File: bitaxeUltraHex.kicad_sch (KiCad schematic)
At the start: 10 parts, among them J1 Screw Terminal, J2 Conn_01x01

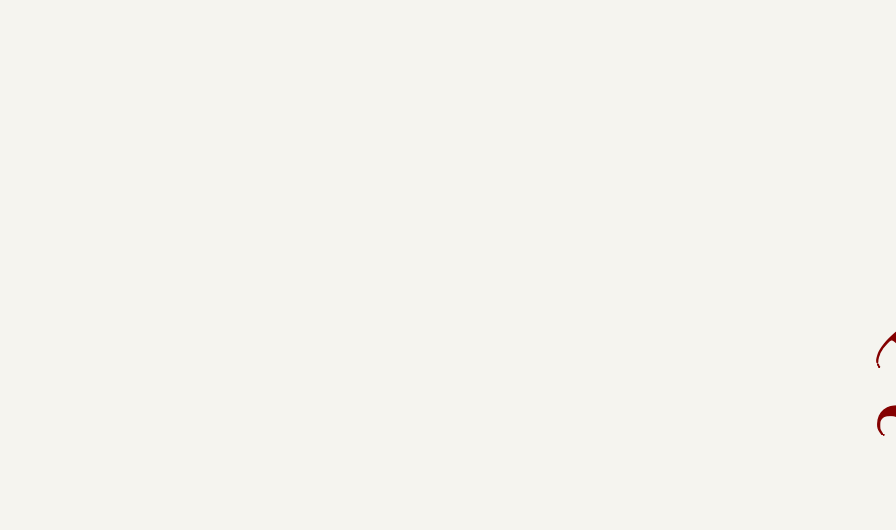
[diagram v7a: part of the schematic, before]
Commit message: re added mounting holes and heatsink mounting holes.
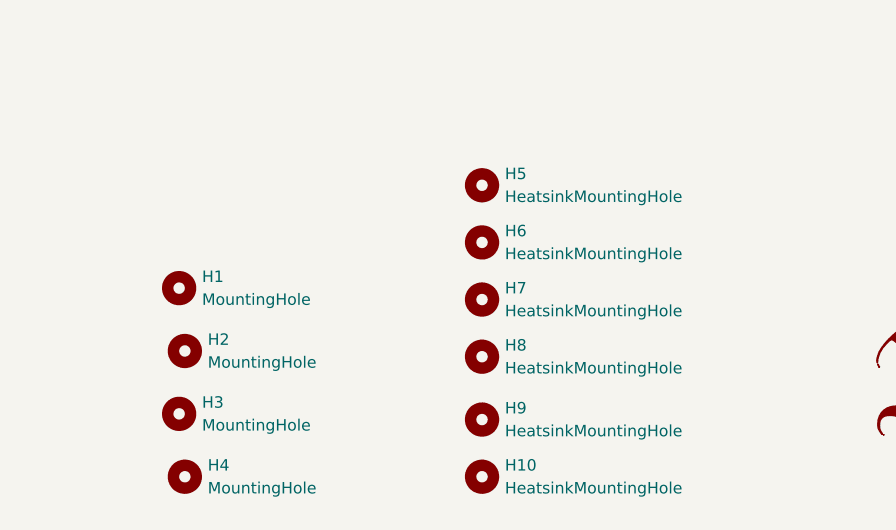
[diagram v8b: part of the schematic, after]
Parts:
- added H1, H2, H3, H4: MountingHole, bitaxe:4mm_mounting, symbol Mechanical:MountingHole
- added H10, H5, H6, H7, H8, H9: HeatsinkMountingHole, bitaxe:2.5mm_mounting, symbol Mechanical:MountingHole
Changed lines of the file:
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@@
+    )
+  )
+  (symbol (lib_id "Mechanical:MountingHole") (at 85.725 190.5 0) (unit 1)
+    (in_bom no) (on_board yes) (dnp no) (fields_autoplaced)
+    (property "Reference" "H4" (at 88.265 189.2299 0)
+      (effects (font (size 1.27 1.27)) (justify left))
+    )
+    (property "Value" "MountingHole" (at 88.265 191.7699 0)
+      (effects (font (size 1.27 1.27)) (justify left))
+    )
+    (property "Footprint" "bitaxe:4mm_mounting" (at 85.725 190.5 0)
+      (effects (font (size 1.27 1.27)) hide)
+    )
+    (property "Datasheet" "~" (at 85.725 190.5 0)
+      (effects (font (size 1.27 1.27)) hide)
+    )
+    (instances
+      (project "bitaxeUltraHex"
+        (path "/e63e39d7-6ac0-4ffd-8aa3-1841a4541b55"
+          (reference "H4") (unit 1)
+        )
+      )
+    )
+  )
+  (symbol (lib_id "Mechanical:MountingHole") (at 85.09 169.545 0) (unit 1)
+    (in_bom no) (on_board yes) (dnp no) (fields_autoplaced)
+    (property "Reference" "H1" (at 87.63 168.2749 0)
+      (effects (font (size 1.27 1.27)) (justify left))
+    )
+    (property "Value" "MountingHole" (at 87.63 170.8149 0)
+      (effects (font (size 1.27 1.27)) (justify left))
+    )
+    (property "Footprint" "bitaxe:4mm_mounting" (at 85.09 169.545 0)
+      (effects (font (size 1.27 1.27)) hide)
+    )
+    (property "Datasheet" "~" (at 85.09 169.545 0)
+      (effects (font (size 1.27 1.27)) hide)
+    )
+    (instances
+      (project "bitaxeUltraHex"
+        (path "/e63e39d7-6ac0-4ffd-8aa3-1841a4541b55"
+          (reference "H1") (unit 1)
+        )
+      )
+    )
+  )
+  (symbol (lib_id "Mechanical:MountingHole") (at 85.725 176.53 0) (unit 1)
+    (in_bom no) (on_board yes) (dnp no) (fields_autoplaced)
+    (property "Reference" "H2" (at 88.265 175.2599 0)
+      (effects (font (size 1.27 1.27)) (justify left))
+    )
+    (property "Value" "MountingHole" (at 88.265 177.7999 0)
+      (effects (font (size 1.27 1.27)) (justify left))
+    )
+    (property "Footprint" "bitaxe:4mm_mounting" (at 85.725 176.53 0)
+      (effects (font (size 1.27 1.27)) hide)
+    )
+    (property "Datasheet" "~" (at 85.725 176.53 0)
+      (effects (font (size 1.27 1.27)) hide)
+    )
+    (instances
+      (project "bitaxeUltraHex"
+        (path "/e63e39d7-6ac0-4ffd-8aa3-1841a4541b55"
+          (reference "H2") (unit 1)
+        )
+      )
     )
   )
@@
     )
   )
+  (symbol (lib_id "Mechanical:MountingHole") (at 85.09 183.515 0) (unit 1)
+    (in_bom no) (on_board yes) (dnp no) (fields_autoplaced)
+    (property "Reference" "H3" (at 87.63 182.2449 0)
+      (effects (font (size 1.27 1.27)) (justify left))
+    )
+    (property "Value" "MountingHole" (at 87.63 184.7849 0)
+      (effects (font (size 1.27 1.27)) (justify left))
+    )
+    (property "Footprint" "bitaxe:4mm_mounting" (at 85.09 183.515 0)
+      (effects (font (size 1.27 1.27)) hide)
+    )
+    (property "Datasheet" "~" (at 85.09 183.515 0)
+      (effects (font (size 1.27 1.27)) hide)
+    )
+    (instances
+      (project "bitaxeUltraHex"
+        (path "/e63e39d7-6ac0-4ffd-8aa3-1841a4541b55"
+          (reference "H3") (unit 1)
+        )
+      )
+    )
+  )
   (symbol (lib_id "Mechanical:Fiducial") (at 53.975 178.435 0) (unit 1)
     (in_bom no) (on_board yes) (dnp no) (fields_autoplaced)
@@
         (path "/e63e39d7-6ac0-4ffd-8aa3-1841a4541b55"
           (reference "FID6") (unit 1)
+        )
+      )
+    )
+  )
+  (symbol (lib_id "Mechanical:MountingHole") (at 118.745 164.465 0) (unit 1)
+    (in_bom no) (on_board yes) (dnp no) (fields_autoplaced)
+    (property "Reference" "H6" (at 121.285 163.1949 0)
+      (effects (font (size 1.27 1.27)) (justify left))
+    )
+    (property "Value" "HeatsinkMountingHole" (at 121.285 165.7349 0)
+      (effects (font (size 1.27 1.27)) (justify left))
+    )
+    (property "Footprint" "bitaxe:2.5mm_mounting" (at 118.745 164.465 0)
+      (effects (font (size 1.27 1.27)) hide)
+    )
+    (property "Datasheet" "~" (at 118.745 164.465 0)
+      (effects (font (size 1.27 1.27)) hide)
+    )
+    (instances
+      (project "bitaxeUltraHex"
+        (path "/e63e39d7-6ac0-4ffd-8aa3-1841a4541b55"
+          (reference "H6") (unit 1)
         )
       )
@@
     )
   )
+  (symbol (lib_id "Mechanical:MountingHole") (at 118.745 170.815 0) (unit 1)
+    (in_bom no) (on_board yes) (dnp no) (fields_autoplaced)
+    (property "Reference" "H7" (at 121.285 169.5449 0)
+      (effects (font (size 1.27 1.27)) (justify left))
+    )
+    (property "Value" "HeatsinkMountingHole" (at 121.285 172.0849 0)
+      (effects (font (size 1.27 1.27)) (justify left))
+    )
+    (property "Footprint" "bitaxe:2.5mm_mounting" (at 118.745 170.815 0)
+      (effects (font (size 1.27 1.27)) hide)
+    )
+    (property "Datasheet" "~" (at 118.745 170.815 0)
+      (effects (font (size 1.27 1.27)) hide)
+    )
+    (instances
+      (project "bitaxeUltraHex"
+        (path "/e63e39d7-6ac0-4ffd-8aa3-1841a4541b55"
+          (reference "H7") (unit 1)
+        )
+      )
+    )
+  )
   (symbol (lib_id "Mechanical:Fiducial") (at 37.465 184.785 0) (unit 1)
     (in_bom no) (on_board yes) (dnp no) (fields_autoplaced)
@@
     )
   )
+  (symbol (lib_id "Mechanical:MountingHole") (at 118.745 158.115 0) (unit 1)
+    (in_bom no) (on_board yes) (dnp no) (fields_autoplaced)
+    (property "Reference" "H5" (at 121.285 156.8449 0)
+      (effects (font (size 1.27 1.27)) (justify left))
+    )
+    (property "Value" "HeatsinkMountingHole" (at 121.285 159.3849 0)
+      (effects (font (size 1.27 1.27)) (justify left))
+    )
+    (property "Footprint" "bitaxe:2.5mm_mounting" (at 118.745 158.115 0)
+      (effects (font (size 1.27 1.27)) hide)
+    )
+    (property "Datasheet" "~" (at 118.745 158.115 0)
+      (effects (font (size 1.27 1.27)) hide)
+    )
+    (instances
+      (project "bitaxeUltraHex"
+        (path "/e63e39d7-6ac0-4ffd-8aa3-1841a4541b55"
+          (reference "H5") (unit 1)
+        )
+      )
+    )
+  )
   (symbol (lib_id "Mechanical:Fiducial") (at 53.975 191.135 0) (unit 1)
     (in_bom no) (on_board yes) (dnp no) (fields_autoplaced)
@@
     )
   )
+  (symbol (lib_id "Mechanical:MountingHole") (at 118.745 177.165 0) (unit 1)
+    (in_bom no) (on_board yes) (dnp no) (fields_autoplaced)
+    (property "Reference" "H8" (at 121.285 175.8949 0)
+      (effects (font (size 1.27 1.27)) (justify left))
+    )
+    (property "Value" "HeatsinkMountingHole" (at 121.285 178.4349 0)
+      (effects (font (size 1.27 1.27)) (justify left))
+    )
+    (property "Footprint" "bitaxe:2.5mm_mounting" (at 118.745 177.165 0)
+      (effects (font (size 1.27 1.27)) hide)
+    )
+    (property "Datasheet" "~" (at 118.745 177.165 0)
+      (effects (font (size 1.27 1.27)) hide)
+    )
+    (instances
+      (project "bitaxeUltraHex"
+        (path "/e63e39d7-6ac0-4ffd-8aa3-1841a4541b55"
+          (reference "H8") (unit 1)
+        )
+      )
+    )
+  )
   (symbol (lib_id "Mechanical:Fiducial") (at 37.465 178.435 0) (unit 1)
     (in_bom no) (on_board yes) (dnp no) (fields_autoplaced)
@@
         )
       )
+    )
+  )
+  (symbol (lib_id "Mechanical:MountingHole") (at 118.745 190.5 0) (unit 1)
+    (in_bom no) (on_board yes) (dnp no) (fields_autoplaced)
+    (property "Reference" "H10" (at 121.285 189.2299 0)
+      (effects (font (size 1.27 1.27)) (justify left))
+    )
+    (property "Value" "HeatsinkMountingHole" (at 121.285 191.7699 0)
+      (effects (font (size 1.27 1.27)) (justify left))
+    )
+    (property "Footprint" "bitaxe:2.5mm_mounting" (at 118.745 190.5 0)
+      (effects (font (size 1.27 1.27)) hide)
+    )
+    (property "Datasheet" "~" (at 118.745 190.5 0)
+      (effects (font (size 1.27 1.27)) hide)
+    )
+    (instances
+      (project "bitaxeUltraHex"
+        (path "/e63e39d7-6ac0-4ffd-8aa3-1841a4541b55"
+          (reference "H10") (unit 1)
+        )
+      )
+    )
+  )
+  (symbol (lib_id "Mechanical:MountingHole") (at 118.745 184.15 0) (unit 1)
+    (in_bom no) (on_board yes) (dnp no) (fields_autoplaced)
+    (property "Reference" "H9" (at 121.285 182.8799 0)
+      (effects (font (size 1.27 1.27)) (justify left))
+    )
+    (property "Value" "HeatsinkMountingHole" (at 121.285 185.4199 0)
+      (effects (font (size 1.27 1.27)) (justify left))
+    )
+    (property "Footprint" "bitaxe:2.5mm_mounting" (at 118.745 184.15 0)
+      (effects (font (size 1.27 1.27)) hide)
+    )
+    (property "Datasheet" "~" (at 118.745 184.15 0)
+      (effects (font (size 1.27 1.27)) hide)
+    )
+    (instances
+      (project "bitaxeUltraHex"
+        (path "/e63e39d7-6ac0-4ffd-8aa3-1841a4541b55"
+          (reference "H9") (unit 1)
+        )
+      )
